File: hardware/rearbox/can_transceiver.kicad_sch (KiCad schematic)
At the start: 9 parts

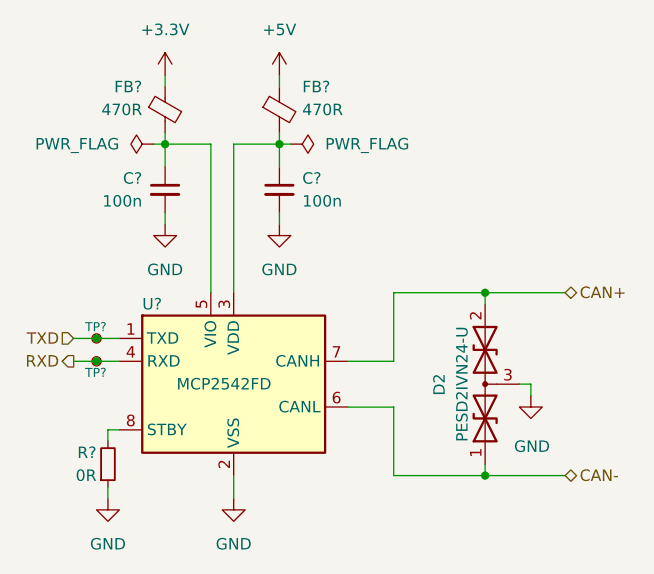
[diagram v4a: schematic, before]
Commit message: Route the tracks on the connector PCB
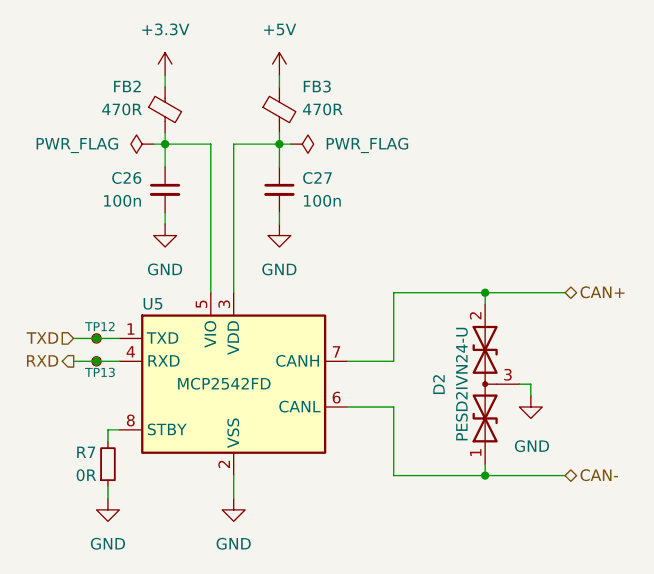
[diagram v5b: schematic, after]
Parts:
- gave numbers to parts that had none: 8
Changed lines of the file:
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@@
   (symbol (lib_id "power:GND") (at 173.99 109.22 0) (unit 1)
     (in_bom yes) (on_board yes) (dnp no)
-    (property "Reference" "#U?" (at 173.99 115.57 0)
+    (property "Reference" "#U01" (at 173.99 115.57 0)
       (effects (font (size 1.27 1.27)) hide)
     )
@@
     (instances
       (project "rearbox"
-        (path "/b652b05a-4e3d-4ad1-b032-18886abe7d45/38408e41-dfb1-4c27-acb0-3f1224cc8789"
-          (reference "#U?") (unit 1)
-        )
         (path "/b652b05a-4e3d-4ad1-b032-18886abe7d45/38408e41-dfb1-4c27-acb0-3f1224cc8789/eec2c93a-0fce-4d3a-ab43-9e1e0481c06c"
           (reference "#U01") (unit 1)
@@
   (symbol (lib_id "Device:C_Small") (at 133.35 86.36 0) (mirror y) (unit 1)
     (in_bom yes) (on_board yes) (dnp no)
-    (property "Reference" "C?" (at 130.81 85.09 0)
+    (property "Reference" "C26" (at 130.81 85.09 0)
       (effects (font (size 1.27 1.27)) (justify left))
     )
@@
     (instances
       (project "rearbox"
-        (path "/b652b05a-4e3d-4ad1-b032-18886abe7d45/38408e41-dfb1-4c27-acb0-3f1224cc8789"
-          (reference "C?") (unit 1)
-        )
         (path "/b652b05a-4e3d-4ad1-b032-18886abe7d45/38408e41-dfb1-4c27-acb0-3f1224cc8789/eec2c93a-0fce-4d3a-ab43-9e1e0481c06c"
           (reference "C26") (unit 1)
@@
   (symbol (lib_id "Connector:TestPoint_Small") (at 125.73 102.87 0) (unit 1)
     (in_bom yes) (on_board yes) (dnp no)
-    (property "Reference" "TP?" (at 124.46 101.6 0)
+    (property "Reference" "TP12" (at 124.46 101.6 0)
       (effects (font (size 1 1)) (justify left))
     )
@@
     (instances
       (project "rearbox"
-        (path "/b652b05a-4e3d-4ad1-b032-18886abe7d45/38408e41-dfb1-4c27-acb0-3f1224cc8789"
-          (reference "TP?") (unit 1)
-        )
         (path "/b652b05a-4e3d-4ad1-b032-18886abe7d45/38408e41-dfb1-4c27-acb0-3f1224cc8789/eec2c93a-0fce-4d3a-ab43-9e1e0481c06c"
           (reference "TP12") (unit 1)
@@
   (symbol (lib_id "power:+3.3V") (at 133.35 73.66 0) (unit 1)
     (in_bom yes) (on_board yes) (dnp no)
-    (property "Reference" "#PWR?" (at 133.35 77.47 0)
+    (property "Reference" "#PWR060" (at 133.35 77.47 0)
       (effects (font (size 1.27 1.27)) hide)
     )
@@
     (instances
       (project "rearbox"
-        (path "/b652b05a-4e3d-4ad1-b032-18886abe7d45/38408e41-dfb1-4c27-acb0-3f1224cc8789"
-          (reference "#PWR?") (unit 1)
-        )
         (path "/b652b05a-4e3d-4ad1-b032-18886abe7d45/38408e41-dfb1-4c27-acb0-3f1224cc8789/eec2c93a-0fce-4d3a-ab43-9e1e0481c06c"
           (reference "#PWR060") (unit 1)
@@
   (symbol (lib_id "power:GND") (at 140.97 120.65 0) (unit 1)
     (in_bom yes) (on_board yes) (dnp no)
-    (property "Reference" "#PWR?" (at 140.97 127 0)
+    (property "Reference" "#PWR062" (at 140.97 127 0)
       (effects (font (size 1.27 1.27)) hide)
     )
@@
     (instances
       (project "rearbox"
-        (path "/b652b05a-4e3d-4ad1-b032-18886abe7d45/38408e41-dfb1-4c27-acb0-3f1224cc8789"
-          (reference "#PWR?") (unit 1)
-        )
         (path "/b652b05a-4e3d-4ad1-b032-18886abe7d45/38408e41-dfb1-4c27-acb0-3f1224cc8789/eec2c93a-0fce-4d3a-ab43-9e1e0481c06c"
           (reference "#PWR062") (unit 1)
@@
   (symbol (lib_id "Interface_CAN_LIN:MCP2542FDxMF") (at 140.97 107.95 0) (unit 1)
     (in_bom yes) (on_board yes) (dnp no)
-    (property "Reference" "U?" (at 130.81 99.06 0)
+    (property "Reference" "U5" (at 130.81 99.06 0)
       (effects (font (size 1.27 1.27)) (justify left))
     )
@@
     (instances
       (project "rearbox"
-        (path "/b652b05a-4e3d-4ad1-b032-18886abe7d45/38408e41-dfb1-4c27-acb0-3f1224cc8789"
-          (reference "U?") (unit 1)
-        )
         (path "/b652b05a-4e3d-4ad1-b032-18886abe7d45/38408e41-dfb1-4c27-acb0-3f1224cc8789/eec2c93a-0fce-4d3a-ab43-9e1e0481c06c"
           (reference "U5") (unit 1)
@@
   (symbol (lib_id "Connector:TestPoint_Small") (at 125.73 105.41 0) (mirror x) (unit 1)
     (in_bom yes) (on_board yes) (dnp no)
-    (property "Reference" "TP?" (at 124.46 106.68 0)
+    (property "Reference" "TP13" (at 124.46 106.68 0)
       (effects (font (size 1 1)) (justify left))
     )
@@
     (instances
       (project "rearbox"
-        (path "/b652b05a-4e3d-4ad1-b032-18886abe7d45/38408e41-dfb1-4c27-acb0-3f1224cc8789"
-          (reference "TP?") (unit 1)
-        )
         (path "/b652b05a-4e3d-4ad1-b032-18886abe7d45/38408e41-dfb1-4c27-acb0-3f1224cc8789/eec2c93a-0fce-4d3a-ab43-9e1e0481c06c"
           (reference "TP13") (unit 1)
@@
   (symbol (lib_id "power:GND") (at 133.35 90.17 0) (unit 1)
     (in_bom yes) (on_board yes) (dnp no)
-    (property "Reference" "#PWR?" (at 133.35 96.52 0)
+    (property "Reference" "#PWR061" (at 133.35 96.52 0)
       (effects (font (size 1.27 1.27)) hide)
     )
@@
     (instances
       (project "rearbox"
-        (path "/b652b05a-4e3d-4ad1-b032-18886abe7d45/38408e41-dfb1-4c27-acb0-3f1224cc8789"
-          (reference "#PWR?") (unit 1)
-        )
         (path "/b652b05a-4e3d-4ad1-b032-18886abe7d45/38408e41-dfb1-4c27-acb0-3f1224cc8789/eec2c93a-0fce-4d3a-ab43-9e1e0481c06c"
           (reference "#PWR061") (unit 1)
@@
   (symbol (lib_id "Device:FerriteBead_Small") (at 146.05 77.47 0) (unit 1)
     (in_bom yes) (on_board yes) (dnp no)
-    (property "Reference" "FB?" (at 148.59 74.93 0)
+    (property "Reference" "FB3" (at 148.59 74.93 0)
       (effects (font (size 1.27 1.27)) (justify left))
     )
@@
     (instances
       (project "rearbox"
-        (path "/b652b05a-4e3d-4ad1-b032-18886abe7d45/38408e41-dfb1-4c27-acb0-3f1224cc8789"
-          (reference "FB?") (unit 1)
-        )
         (path "/b652b05a-4e3d-4ad1-b032-18886abe7d45/38408e41-dfb1-4c27-acb0-3f1224cc8789/eec2c93a-0fce-4d3a-ab43-9e1e0481c06c"
           (reference "FB3") (unit 1)
@@
   (symbol (lib_id "Device:C_Small") (at 146.05 86.36 0) (unit 1)
     (in_bom yes) (on_board yes) (dnp no)
-    (property "Reference" "C?" (at 148.59 85.09 0)
+    (property "Reference" "C27" (at 148.59 85.09 0)
       (effects (font (size 1.27 1.27)) (justify left))
     )
@@
     (instances
       (project "rearbox"
-        (path "/b652b05a-4e3d-4ad1-b032-18886abe7d45/38408e41-dfb1-4c27-acb0-3f1224cc8789"
-          (reference "C?") (unit 1)
-        )
         (path "/b652b05a-4e3d-4ad1-b032-18886abe7d45/38408e41-dfb1-4c27-acb0-3f1224cc8789/eec2c93a-0fce-4d3a-ab43-9e1e0481c06c"
           (reference "C27") (unit 1)
@@
   (symbol (lib_id "Device:FerriteBead_Small") (at 133.35 77.47 0) (unit 1)
     (in_bom yes) (on_board yes) (dnp no)
-    (property "Reference" "FB?" (at 130.81 74.93 0)
+    (property "Reference" "FB2" (at 130.81 74.93 0)
       (effects (font (size 1.27 1.27)) (justify right))
     )
@@
     (instances
       (project "rearbox"
-        (path "/b652b05a-4e3d-4ad1-b032-18886abe7d45/38408e41-dfb1-4c27-acb0-3f1224cc8789"
-          (reference "FB?") (unit 1)
-        )
         (path "/b652b05a-4e3d-4ad1-b032-18886abe7d45/38408e41-dfb1-4c27-acb0-3f1224cc8789/eec2c93a-0fce-4d3a-ab43-9e1e0481c06c"
           (reference "FB2") (unit 1)
@@
   (symbol (lib_id "power:GND") (at 146.05 90.17 0) (unit 1)
     (in_bom yes) (on_board yes) (dnp no)
-    (property "Reference" "#PWR?" (at 146.05 96.52 0)
+    (property "Reference" "#PWR064" (at 146.05 96.52 0)
       (effects (font (size 1.27 1.27)) hide)
     )
@@
     (instances
       (project "rearbox"
-        (path "/b652b05a-4e3d-4ad1-b032-18886abe7d45/38408e41-dfb1-4c27-acb0-3f1224cc8789"
-          (reference "#PWR?") (unit 1)
-        )
         (path "/b652b05a-4e3d-4ad1-b032-18886abe7d45/38408e41-dfb1-4c27-acb0-3f1224cc8789/eec2c93a-0fce-4d3a-ab43-9e1e0481c06c"
           (reference "#PWR064") (unit 1)
@@
   (symbol (lib_id "power:GND") (at 127 120.65 0) (unit 1)
     (in_bom yes) (on_board yes) (dnp no)
-    (property "Reference" "#PWR?" (at 127 127 0)
+    (property "Reference" "#PWR059" (at 127 127 0)
       (effects (font (size 1.27 1.27)) hide)
     )
@@
     (instances
       (project "rearbox"
-        (path "/b652b05a-4e3d-4ad1-b032-18886abe7d45/38408e41-dfb1-4c27-acb0-3f1224cc8789"
-          (reference "#PWR?") (unit 1)
-        )
         (path "/b652b05a-4e3d-4ad1-b032-18886abe7d45/38408e41-dfb1-4c27-acb0-3f1224cc8789/eec2c93a-0fce-4d3a-ab43-9e1e0481c06c"
           (reference "#PWR059") (unit 1)
@@
   (symbol (lib_id "Device:R_Small") (at 127 116.84 0) (mirror x) (unit 1)
     (in_bom yes) (on_board yes) (dnp no)
-    (property "Reference" "R?" (at 125.73 115.57 0)
+    (property "Reference" "R7" (at 125.73 115.57 0)
       (effects (font (size 1.27 1.27)) (justify right))
     )
@@
     (instances
       (project "rearbox"
-        (path "/b652b05a-4e3d-4ad1-b032-18886abe7d45/264ec557-c33b-4d6e-8249-7c546f6f500a"
-          (reference "R?") (unit 1)
-        )
-        (path "/b652b05a-4e3d-4ad1-b032-18886abe7d45/5d9671f9-6e77-4376-b4d6-afe9f66a07c2"
-          (reference "R?") (unit 1)
-        )
-        (path "/b652b05a-4e3d-4ad1-b032-18886abe7d45/264ec557-c33b-4d6e-8249-7c546f6f500a/2ebbc597-c328-4a79-a9b9-9ad195d56b16"
-          (reference "R130") (unit 1)
-        )
-        (path "/b652b05a-4e3d-4ad1-b032-18886abe7d45/264ec557-c33b-4d6e-8249-7c546f6f500a/388565cf-56d9-4d05-bbee-ba12b3a092d4"
-          (reference "R140") (unit 1)
-        )
         (path "/b652b05a-4e3d-4ad1-b032-18886abe7d45/38408e41-dfb1-4c27-acb0-3f1224cc8789/f1ed15a3-9302-436f-b25a-713477aeadf3"
           (reference "R7") (unit 1)

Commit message: Fix measurement bridges polarity
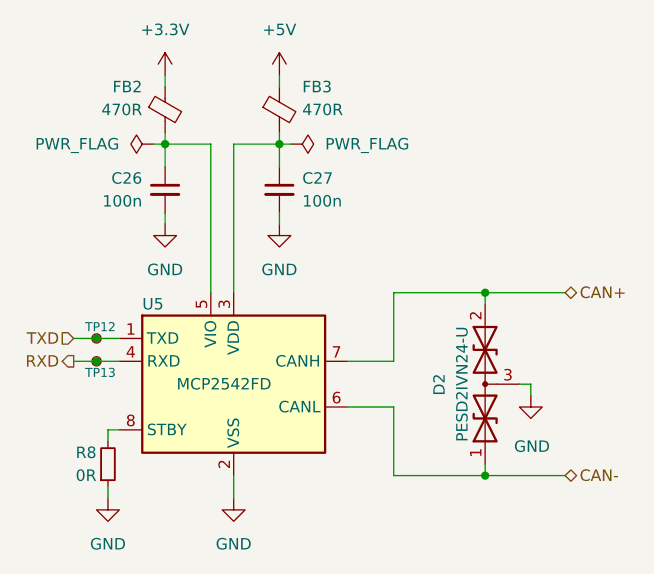
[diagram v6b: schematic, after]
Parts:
- renumbered R7 to R8
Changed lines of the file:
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@@
   (title_block
     (title "CAN Transceiver")
-    (date "2023-11-17")
+    (date "2024-04-28")
     (rev "${REVISION}")
     (company "Author: I. Kajdan")
@@
   (symbol (lib_id "power:+3.3V") (at 133.35 73.66 0) (unit 1)
     (in_bom yes) (on_board yes) (dnp no)
-    (property "Reference" "#PWR060" (at 133.35 77.47 0)
+    (property "Reference" "#PWR061" (at 133.35 77.47 0)
       (effects (font (size 1.27 1.27)) hide)
     )
@@
       (project "rearbox"
         (path "/b652b05a-4e3d-4ad1-b032-18886abe7d45/38408e41-dfb1-4c27-acb0-3f1224cc8789/eec2c93a-0fce-4d3a-ab43-9e1e0481c06c"
-          (reference "#PWR060") (unit 1)
-        )
-        (path "/b652b05a-4e3d-4ad1-b032-18886abe7d45/38408e41-dfb1-4c27-acb0-3f1224cc8789/f1ed15a3-9302-436f-b25a-713477aeadf3"
-          (reference "#PWR066") (unit 1)
+          (reference "#PWR061") (unit 1)
+        )
+        (path "/b652b05a-4e3d-4ad1-b032-18886abe7d45/38408e41-dfb1-4c27-acb0-3f1224cc8789/f1ed15a3-9302-436f-b25a-713477aeadf3"
+          (reference "#PWR067") (unit 1)
         )
       )
@@
   (symbol (lib_id "power:GND") (at 140.97 120.65 0) (unit 1)
     (in_bom yes) (on_board yes) (dnp no)
-    (property "Reference" "#PWR062" (at 140.97 127 0)
+    (property "Reference" "#PWR063" (at 140.97 127 0)
       (effects (font (size 1.27 1.27)) hide)
     )
@@
       (project "rearbox"
         (path "/b652b05a-4e3d-4ad1-b032-18886abe7d45/38408e41-dfb1-4c27-acb0-3f1224cc8789/eec2c93a-0fce-4d3a-ab43-9e1e0481c06c"
-          (reference "#PWR062") (unit 1)
-        )
-        (path "/b652b05a-4e3d-4ad1-b032-18886abe7d45/38408e41-dfb1-4c27-acb0-3f1224cc8789/f1ed15a3-9302-436f-b25a-713477aeadf3"
-          (reference "#PWR068") (unit 1)
+          (reference "#PWR063") (unit 1)
+        )
+        (path "/b652b05a-4e3d-4ad1-b032-18886abe7d45/38408e41-dfb1-4c27-acb0-3f1224cc8789/f1ed15a3-9302-436f-b25a-713477aeadf3"
+          (reference "#PWR069") (unit 1)
         )
       )
@@
   (symbol (lib_id "power:GND") (at 133.35 90.17 0) (unit 1)
     (in_bom yes) (on_board yes) (dnp no)
-    (property "Reference" "#PWR061" (at 133.35 96.52 0)
+    (property "Reference" "#PWR062" (at 133.35 96.52 0)
       (effects (font (size 1.27 1.27)) hide)
     )
@@
       (project "rearbox"
         (path "/b652b05a-4e3d-4ad1-b032-18886abe7d45/38408e41-dfb1-4c27-acb0-3f1224cc8789/eec2c93a-0fce-4d3a-ab43-9e1e0481c06c"
-          (reference "#PWR061") (unit 1)
-        )
-        (path "/b652b05a-4e3d-4ad1-b032-18886abe7d45/38408e41-dfb1-4c27-acb0-3f1224cc8789/f1ed15a3-9302-436f-b25a-713477aeadf3"
-          (reference "#PWR067") (unit 1)
+          (reference "#PWR062") (unit 1)
+        )
+        (path "/b652b05a-4e3d-4ad1-b032-18886abe7d45/38408e41-dfb1-4c27-acb0-3f1224cc8789/f1ed15a3-9302-436f-b25a-713477aeadf3"
+          (reference "#PWR068") (unit 1)
         )
       )
@@
   (symbol (lib_id "power:+5V") (at 146.05 73.66 0) (unit 1)
     (in_bom yes) (on_board yes) (dnp no) (fields_autoplaced)
-    (property "Reference" "#PWR063" (at 146.05 77.47 0)
+    (property "Reference" "#PWR064" (at 146.05 77.47 0)
       (effects (font (size 1.27 1.27)) hide)
     )
@@
       (project "rearbox"
         (path "/b652b05a-4e3d-4ad1-b032-18886abe7d45/38408e41-dfb1-4c27-acb0-3f1224cc8789/eec2c93a-0fce-4d3a-ab43-9e1e0481c06c"
-          (reference "#PWR063") (unit 1)
-        )
-        (path "/b652b05a-4e3d-4ad1-b032-18886abe7d45/38408e41-dfb1-4c27-acb0-3f1224cc8789/f1ed15a3-9302-436f-b25a-713477aeadf3"
-          (reference "#PWR069") (unit 1)
+          (reference "#PWR064") (unit 1)
+        )
+        (path "/b652b05a-4e3d-4ad1-b032-18886abe7d45/38408e41-dfb1-4c27-acb0-3f1224cc8789/f1ed15a3-9302-436f-b25a-713477aeadf3"
+          (reference "#PWR070") (unit 1)
         )
       )
@@
   (symbol (lib_id "power:GND") (at 146.05 90.17 0) (unit 1)
     (in_bom yes) (on_board yes) (dnp no)
-    (property "Reference" "#PWR064" (at 146.05 96.52 0)
+    (property "Reference" "#PWR065" (at 146.05 96.52 0)
       (effects (font (size 1.27 1.27)) hide)
     )
@@
       (project "rearbox"
         (path "/b652b05a-4e3d-4ad1-b032-18886abe7d45/38408e41-dfb1-4c27-acb0-3f1224cc8789/eec2c93a-0fce-4d3a-ab43-9e1e0481c06c"
-          (reference "#PWR064") (unit 1)
-        )
-        (path "/b652b05a-4e3d-4ad1-b032-18886abe7d45/38408e41-dfb1-4c27-acb0-3f1224cc8789/f1ed15a3-9302-436f-b25a-713477aeadf3"
-          (reference "#PWR070") (unit 1)
+          (reference "#PWR065") (unit 1)
+        )
+        (path "/b652b05a-4e3d-4ad1-b032-18886abe7d45/38408e41-dfb1-4c27-acb0-3f1224cc8789/f1ed15a3-9302-436f-b25a-713477aeadf3"
+          (reference "#PWR071") (unit 1)
         )
       )
@@
   (symbol (lib_id "power:GND") (at 127 120.65 0) (unit 1)
     (in_bom yes) (on_board yes) (dnp no)
-    (property "Reference" "#PWR059" (at 127 127 0)
+    (property "Reference" "#PWR060" (at 127 127 0)
       (effects (font (size 1.27 1.27)) hide)
     )
@@
       (project "rearbox"
         (path "/b652b05a-4e3d-4ad1-b032-18886abe7d45/38408e41-dfb1-4c27-acb0-3f1224cc8789/eec2c93a-0fce-4d3a-ab43-9e1e0481c06c"
-          (reference "#PWR059") (unit 1)
-        )
-        (path "/b652b05a-4e3d-4ad1-b032-18886abe7d45/38408e41-dfb1-4c27-acb0-3f1224cc8789/f1ed15a3-9302-436f-b25a-713477aeadf3"
-          (reference "#PWR065") (unit 1)
+          (reference "#PWR060") (unit 1)
+        )
+        (path "/b652b05a-4e3d-4ad1-b032-18886abe7d45/38408e41-dfb1-4c27-acb0-3f1224cc8789/f1ed15a3-9302-436f-b25a-713477aeadf3"
+          (reference "#PWR066") (unit 1)
         )
       )
@@
   (symbol (lib_id "Device:R_Small") (at 127 116.84 0) (mirror x) (unit 1)
     (in_bom yes) (on_board yes) (dnp no)
-    (property "Reference" "R7" (at 125.73 115.57 0)
+    (property "Reference" "R8" (at 125.73 115.57 0)
       (effects (font (size 1.27 1.27)) (justify right))
     )
@@
       (project "rearbox"
         (path "/b652b05a-4e3d-4ad1-b032-18886abe7d45/38408e41-dfb1-4c27-acb0-3f1224cc8789/f1ed15a3-9302-436f-b25a-713477aeadf3"
+          (reference "R8") (unit 1)
+        )
+        (path "/b652b05a-4e3d-4ad1-b032-18886abe7d45/38408e41-dfb1-4c27-acb0-3f1224cc8789/eec2c93a-0fce-4d3a-ab43-9e1e0481c06c"
           (reference "R7") (unit 1)
         )
-        (path "/b652b05a-4e3d-4ad1-b032-18886abe7d45/38408e41-dfb1-4c27-acb0-3f1224cc8789/eec2c93a-0fce-4d3a-ab43-9e1e0481c06c"
-          (reference "R6") (unit 1)
-        )
-      )
+      )
